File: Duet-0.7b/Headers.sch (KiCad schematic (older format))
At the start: 14 parts, among them J1 EXPANSION, J10 E0 MOT/STOP, J2 CONN2, J20 5V_PS, J23 POWER IN, J24 GND V_IN, J28 Probe, J4 BED HEATER, J5 BED TEMP, J6 CONN2, J7 Z MOT/STOP, J8 Y MOT/STOP, J9 X MOT/STOP, P1 CONN_4

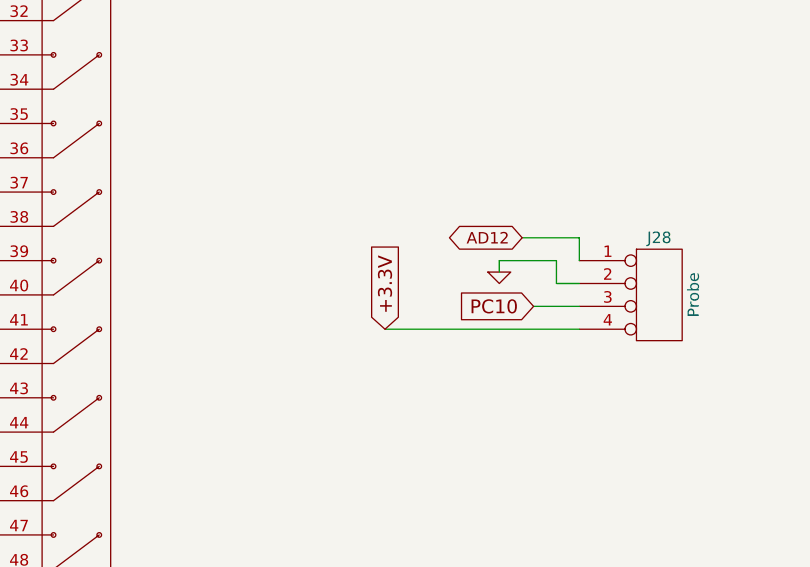
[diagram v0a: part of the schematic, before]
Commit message: Power connector changed to 7.5mm pitch and nearby components moved to accommodate that.  10u capacitor added across the power supply to the probe socket.
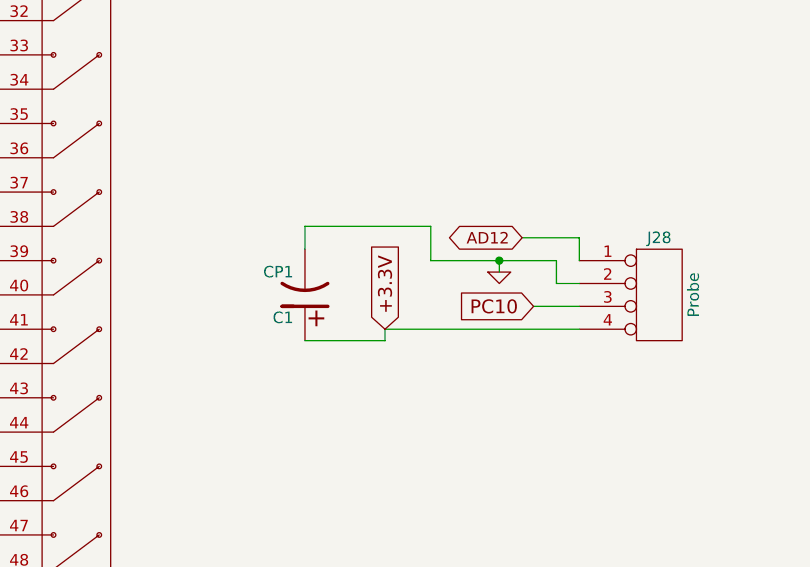
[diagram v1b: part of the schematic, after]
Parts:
- added C1: CP1, ~, symbol CP1
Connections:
- net +3.3V: now also C1.1
- net GND: now also C1.2
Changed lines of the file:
@@
 Sheet 4 7
 Title "Duet"
-Date "17 dec 2014"
+Date "16 jan 2015"
 Rev "0.7"
 Comp "Think3DPrint3D, RepRapPro"
@@
 	4100 6450 4100 6400
 Wire Wire Line
-	4100 6400 4350 6400
+	3800 6400 4350 6400
 Wire Wire Line
 	4350 6400 4350 6500
@@
 Wire Wire Line
 	9450 6350 9850 6350
+$Comp
+L CP1 C1
+U 1 1 54B946B7
+P 3250 6550
+F 0 "C1" H 3300 6650 50  0000 L CNN
+F 1 "CP1" H 3300 6450 50  0000 L CNN
+F 2 "~" H 3250 6550 60  0000 C CNN
+F 3 "~" H 3250 6550 60  0000 C CNN
+	1    3250 6550
+	-1   0    0    1
+$EndComp
+Wire Wire Line
+	3600 6700 3600 6750
+Wire Wire Line
+	3600 6750 3250 6750
+Wire Wire Line
+	3800 6400 3800 6250
+Wire Wire Line
+	3800 6250 3250 6250
+Wire Wire Line
+	3250 6250 3250 6350
+Connection ~ 4100 6400
 $EndSCHEMATC
